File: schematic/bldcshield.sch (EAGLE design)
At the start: 39 parts, among them IC1 IR2101SMD, IC2 IR2101SMD, IC3 IR2101SMD, Q1 MOSFET-NCHANNELFDD8580, Q2 MOSFET-NCHANNELFDD8580, Q3 Shield, Q4 MOSFET-NCHANNELFDD8580, Q5 MOSFET-NCHANNELFDD8580, Q6 MOSFET-NCHANNELFDD8580, Q7 MOSFET-NCHANNELFDD8580, U3 LM317DCY, X1 MKDSN1,5/2-5,08, X2 MKDSN1,5/3-5,08

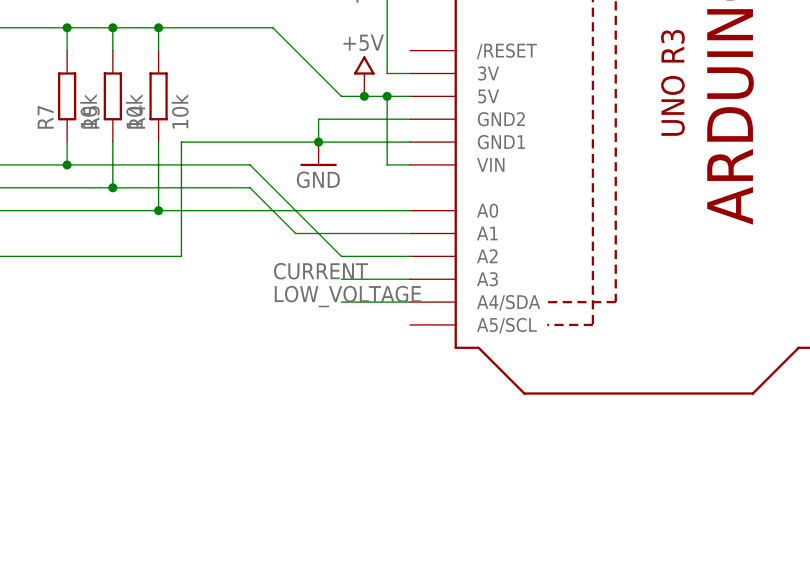
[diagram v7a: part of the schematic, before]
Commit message: change fets to dpaks and changed the layout with multiple pours.
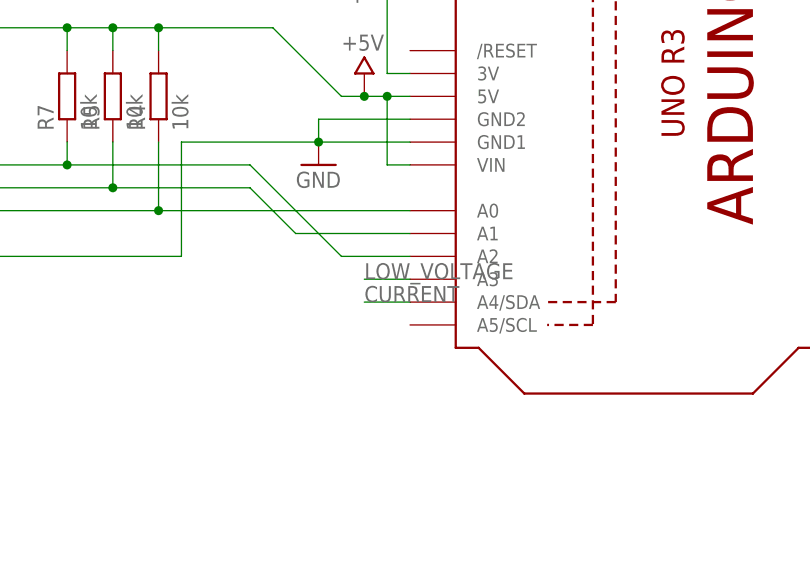
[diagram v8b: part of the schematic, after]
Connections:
- net CURRENT: now also Q3.A4/SDA; no longer Q3.A3
- net LOW_VOLTAGE: now also Q3.A3; no longer Q3.A4/SDA
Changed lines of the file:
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@@
 <grid distance="0.1" unitdist="inch" unit="inch" style="lines" multiple="1" display="no" altdistance="0.01" altunitdist="inch" altunit="inch"/>
 <layers>
-<layer number="1" name="Top" color="4" fill="1" visible="yes" active="no"/>
-<layer number="2" name="Route2" color="1" fill="3" visible="yes" active="no"/>
-<layer number="3" name="Route3" color="4" fill="3" visible="yes" active="no"/>
-<layer number="4" name="Route4" color="1" fill="4" visible="yes" active="no"/>
-<layer number="5" name="Route5" color="4" fill="4" visible="yes" active="no"/>
-<layer number="6" name="Route6" color="1" fill="8" visible="yes" active="no"/>
-<layer number="7" name="Route7" color="4" fill="8" visible="yes" active="no"/>
-<layer number="8" name="Route8" color="1" fill="2" visible="yes" active="no"/>
-<layer number="9" name="Route9" color="4" fill="2" visible="yes" active="no"/>
-<layer number="10" name="Route10" color="1" fill="7" visible="yes" active="no"/>
-<layer number="11" name="Route11" color="4" fill="7" visible="yes" active="no"/>
-<layer number="12" name="Route12" color="1" fill="5" visible="yes" active="no"/>
-<layer number="13" name="Route13" color="4" fill="5" visible="yes" active="no"/>
-<layer number="14" name="Route14" color="1" fill="6" visible="yes" active="no"/>
-<layer number="15" name="Route15" color="4" fill="6" visible="yes" active="no"/>
-<layer number="16" name="Bottom" color="1" fill="1" visible="yes" active="no"/>
-<layer number="17" name="Pads" color="2" fill="1" visible="yes" active="no"/>
-<layer number="18" name="Vias" color="2" fill="1" visible="yes" active="no"/>
-<layer number="19" name="Unrouted" color="6" fill="1" visible="yes" active="no"/>
-<layer number="20" name="Dimension" color="15" fill="1" visible="yes" active="no"/>
-<layer number="21" name="tPlace" color="7" fill="1" visible="yes" active="no"/>
-<layer number="22" name="bPlace" color="7" fill="1" visible="yes" active="no"/>
-<layer number="23" name="tOrigins" color="15" fill="1" visible="yes" active="no"/>
-<layer number="24" name="bOrigins" color="15" fill="1" visible="yes" active="no"/>
-<layer number="25" name="tNames" color="7" fill="1" visible="yes" active="no"/>
-<layer number="26" name="bNames" color="7" fill="1" visible="yes" active="no"/>
-<layer number="27" name="tValues" color="7" fill="1" visible="yes" active="no"/>
-<layer number="28" name="bValues" color="7" fill="1" visible="yes" active="no"/>
+<layer number="1" name="Top" color="4" fill="1" visible="no" active="no"/>
+<layer number="2" name="Route2" color="1" fill="3" visible="no" active="no"/>
+<layer number="3" name="Route3" color="4" fill="3" visible="no" active="no"/>
+<layer number="4" name="Route4" color="1" fill="4" visible="no" active="no"/>
+<layer number="5" name="Route5" color="4" fill="4" visible="no" active="no"/>
+<layer number="6" name="Route6" color="1" fill="8" visible="no" active="no"/>
+<layer number="7" name="Route7" color="4" fill="8" visible="no" active="no"/>
+<layer number="8" name="Route8" color="1" fill="2" visible="no" active="no"/>
+<layer number="9" name="Route9" color="4" fill="2" visible="no" active="no"/>
+<layer number="10" name="Route10" color="1" fill="7" visible="no" active="no"/>
+<layer number="11" name="Route11" color="4" fill="7" visible="no" active="no"/>
+<layer number="12" name="Route12" color="1" fill="5" visible="no" active="no"/>
+<layer number="13" name="Route13" color="4" fill="5" visible="no" active="no"/>
+<layer number="14" name="Route14" color="1" fill="6" visible="no" active="no"/>
+<layer number="15" name="Route15" color="4" fill="6" visible="no" active="no"/>
+<layer number="16" name="Bottom" color="1" fill="1" visible="no" active="no"/>
+<layer number="17" name="Pads" color="2" fill="1" visible="no" active="no"/>
+<layer number="18" name="Vias" color="2" fill="1" visible="no" active="no"/>
+<layer number="19" name="Unrouted" color="6" fill="1" visible="no" active="no"/>
+<layer number="20" name="Dimension" color="15" fill="1" visible="no" active="no"/>
+<layer number="21" name="tPlace" color="7" fill="1" visible="no" active="no"/>
+<layer number="22" name="bPlace" color="7" fill="1" visible="no" active="no"/>
+<layer number="23" name="tOrigins" color="15" fill="1" visible="no" active="no"/>
+<layer number="24" name="bOrigins" color="15" fill="1" visible="no" active="no"/>
+<layer number="25" name="tNames" color="7" fill="1" visible="no" active="no"/>
+<layer number="26" name="bNames" color="7" fill="1" visible="no" active="no"/>
+<layer number="27" name="tValues" color="7" fill="1" visible="no" active="no"/>
+<layer number="28" name="bValues" color="7" fill="1" visible="no" active="no"/>
 <layer number="29" name="tStop" color="7" fill="3" visible="no" active="no"/>
 <layer number="30" name="bStop" color="7" fill="6" visible="no" active="no"/>
@@
 <layer number="35" name="tGlue" color="7" fill="4" visible="no" active="no"/>
 <layer number="36" name="bGlue" color="7" fill="5" visible="no" active="no"/>
-<layer number="37" name="tTest" color="7" fill="1" visible="yes" active="no"/>
-<layer number="38" name="bTest" color="7" fill="1" visible="yes" active="no"/>
+<layer number="37" name="tTest" color="7" fill="1" visible="no" active="no"/>
+<layer number="38" name="bTest" color="7" fill="1" visible="no" active="no"/>
 <layer number="39" name="tKeepout" color="4" fill="11" visible="no" active="no"/>
 <layer number="40" name="bKeepout" color="1" fill="11" visible="no" active="no"/>
@@
 <layer number="44" name="Drills" color="7" fill="1" visible="no" active="no"/>
 <layer number="45" name="Holes" color="7" fill="1" visible="no" active="no"/>
-<layer number="46" name="Milling" color="3" fill="1" visible="yes" active="no"/>
-<layer number="47" name="Measures" color="7" fill="1" visible="yes" active="no"/>
-<layer number="48" name="Document" color="7" fill="1" visible="yes" active="no"/>
-<layer number="49" name="Reference" color="7" fill="1" visible="yes" active="no"/>
-<layer number="50" name="dxf" color="12" fill="1" visible="yes" active="no"/>
-<layer number="51" name="tDocu" color="7" fill="1" visible="yes" active="no"/>
-<layer number="52" name="bDocu" color="7" fill="1" visible="yes" active="no"/>
-<layer number="53" name="tGND_GNDA" color="7" fill="1" visible="yes" active="no"/>
-<layer number="54" name="bGND_GNDA" color="7" fill="1" visible="yes" active="no"/>
-<layer number="56" name="wert" color="7" fill="1" visible="yes" active="no"/>
-<layer number="57" name="tCAD" color="7" fill="1" visible="yes" active="no"/>
+<layer number="46" name="Milling" color="3" fill="1" visible="no" active="no"/>
+<layer number="47" name="Measures" color="7" fill="1" visible="no" active="no"/>
+<layer number="48" name="Document" color="7" fill="1" visible="no" active="no"/>
+<layer number="49" name="Reference" color="7" fill="1" visible="no" active="no"/>
+<layer number="50" name="dxf" color="12" fill="1" visible="no" active="no"/>
+<layer number="51" name="tDocu" color="7" fill="1" visible="no" active="no"/>
+<layer number="52" name="bDocu" color="7" fill="1" visible="no" active="no"/>
+<layer number="53" name="tGND_GNDA" color="7" fill="1" visible="no" active="no"/>
+<layer number="54" name="bGND_GNDA" color="7" fill="1" visible="no" active="no"/>
+<layer number="56" name="wert" color="7" fill="1" visible="no" active="no"/>
+<layer number="57" name="tCAD" color="7" fill="1" visible="no" active="no"/>
 <layer number="90" name="Modules" color="5" fill="1" visible="yes" active="yes"/>
 <layer number="91" name="Nets" color="2" fill="1" visible="yes" active="yes"/>
@@
 </segment>
 <segment>
-<wire x1="-236.22" y1="81.28" x2="-243.84" y2="81.28" width="0.1524" layer="91"/>
-<pinref part="Q3" gate="G$1" pin="A3"/>
-<label x="-251.46" y="81.28" size="1.778" layer="95"/>
+<pinref part="Q3" gate="G$1" pin="A4/SDA"/>
+<wire x1="-236.22" y1="78.74" x2="-241.3" y2="78.74" width="0.1524" layer="91"/>
+<label x="-241.3" y="78.74" size="1.778" layer="95"/>
 </segment>
 </net>
@@
 </segment>
 <segment>
-<wire x1="-236.22" y1="78.74" x2="-243.84" y2="78.74" width="0.1524" layer="91"/>
-<label x="-251.46" y="78.74" size="1.778" layer="95"/>
-<pinref part="Q3" gate="G$1" pin="A4/SDA"/>
-</segment>
-</net>
+<pinref part="Q3" gate="G$1" pin="A3"/>
+<wire x1="-236.22" y1="81.28" x2="-241.3" y2="81.28" width="0.1524" layer="91"/>
+<label x="-241.3" y="81.28" size="1.778" layer="95"/>
+</segment>
+</net>
